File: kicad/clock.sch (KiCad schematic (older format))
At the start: 26 parts, among them SW1 SW_Push, SW2 SW_SPDT, U10 74LS08, U11 74LS04, U12 74LS32, U13 74LS08, U14 74LS04, U15 74LS08, U16 74LS04, U7 LM555, U8 LM555, U9 LM555

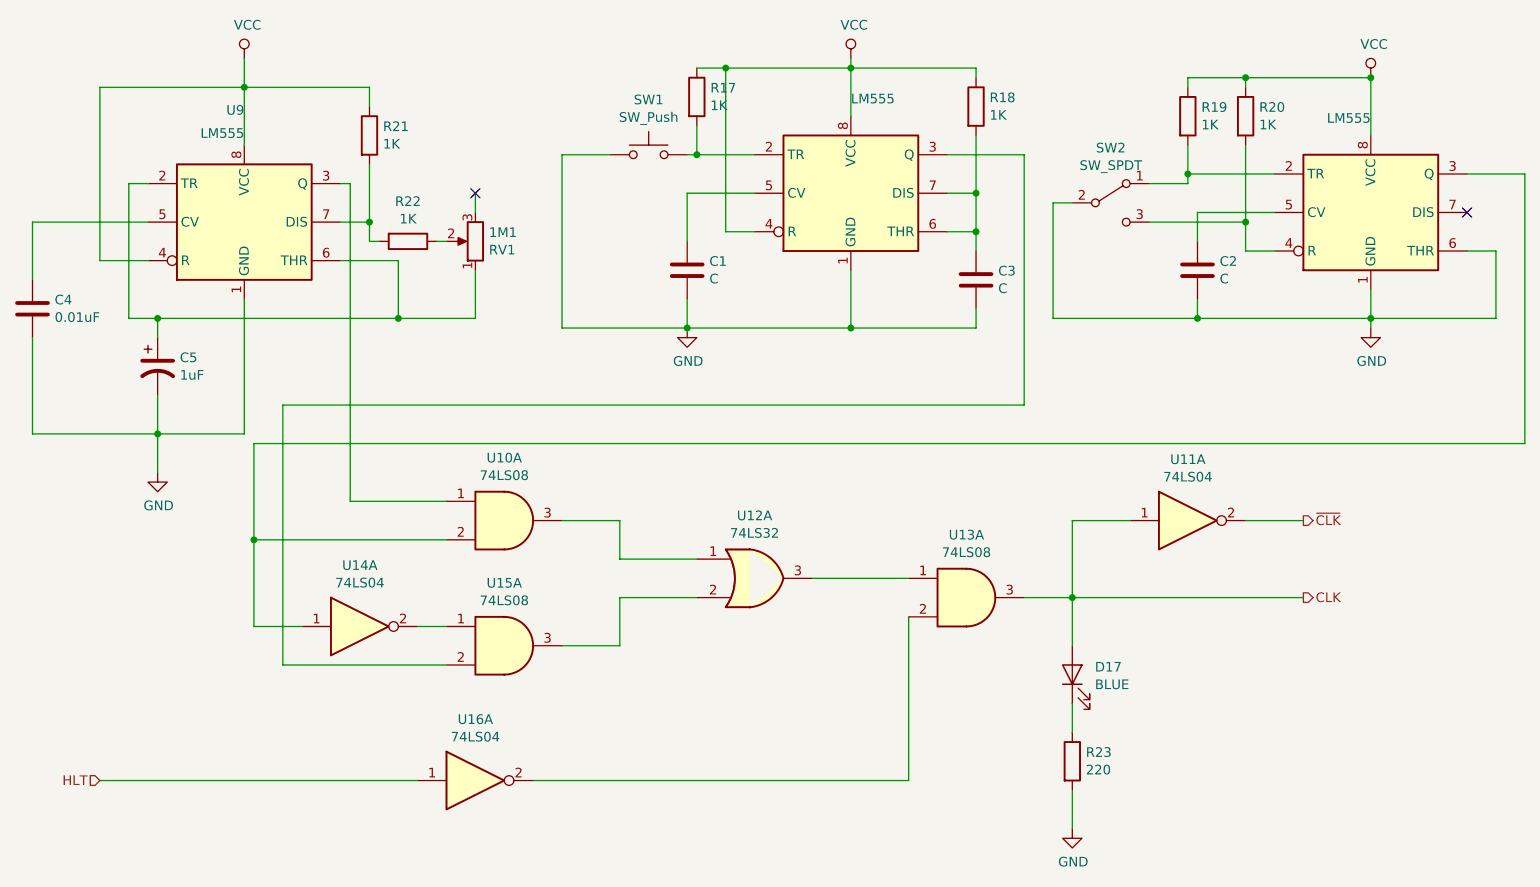
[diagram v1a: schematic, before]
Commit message: Reorganize part references
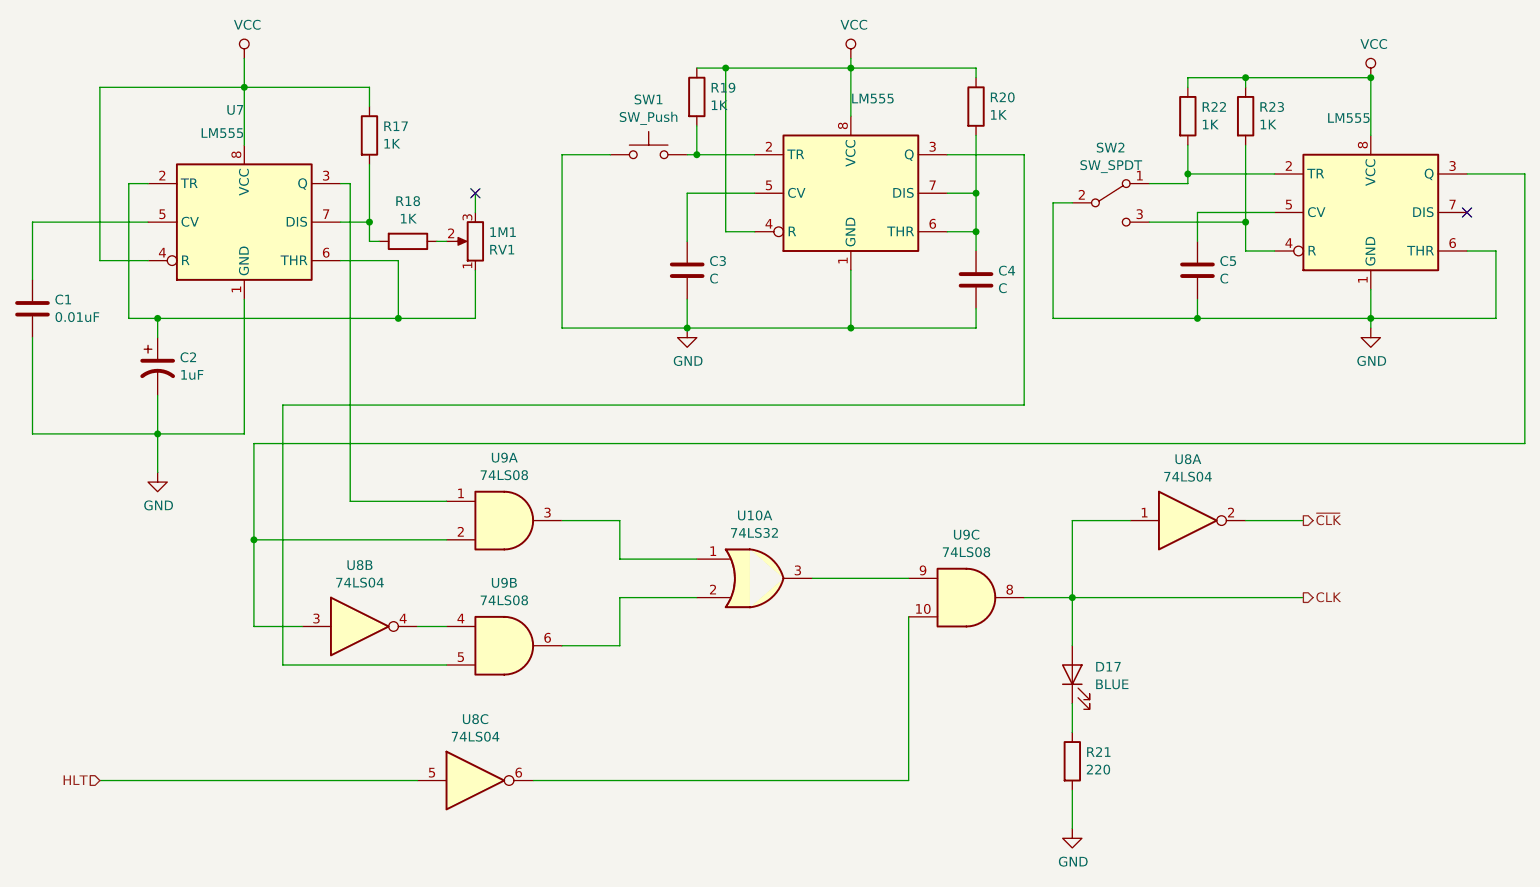
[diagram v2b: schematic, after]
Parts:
- renumbered C4 to C1, C5 to C2, C1 to C3, C3 to C4, C2 to C5, R21 to R17, R22 to R18, R17 to R19, R18 to R20, R23 to R21, R19 to R22, R20 to R23, U12 to U10, U7 to U11, U8 to U12, U9 to U7, U16 to U8, U14 to U8, U11 to U8, U10 to U9, U15 to U9, U13 to U9
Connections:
- net CLK: now also U9.8; no longer U9.3
- net HLT: now also U8.5; no longer U8.1
- net at U11.3 (Q): now also U9.5; no longer U9.2
- net at U12.3 (Q), U9.2: now also U8.3; no longer U8.1
- net at U10.2: now also U9.6; no longer U9.3
- net at U10.3: now also U9.9; no longer U9.1
- new net: U8.4, U9.4
- new net: U8.6, U9.10
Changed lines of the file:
@@
 AR Path="/5D7B7AE3/5D8B6D3B" Ref="U?"  Part="1"
 AR Path="/5DA98D6D/5DA9A52D/5D8B6D3B" Ref="U?"  Part="1"
-AR Path="/5DA9BE9A/5D8B6D3B" Ref="U11"  Part="1"
-F 0 "U11" H 7800 4117 50  0000 C CNN
+AR Path="/5DA9BE9A/5D8B6D3B" Ref="U8"  Part="1"
+F 0 "U8" H 7800 4117 50  0000 C CNN
 F 1 "74LS04" H 7800 4026 50  0000 C CNN
 F 2 "" H 7800 3800 50  0001 C CNN
@@
 AR Path="/5D7B7AE3/5D860CC7" Ref="R?"  Part="1"
 AR Path="/5DA98D6D/5DA9A52D/5D860CC7" Ref="R?"  Part="1"
-AR Path="/5DA9BE9A/5D860CC7" Ref="R23"  Part="1"
-F 0 "R23" H 7270 5096 50  0000 L CNN
+AR Path="/5DA9BE9A/5D860CC7" Ref="R21"  Part="1"
+F 0 "R21" H 7270 5096 50  0000 L CNN
 F 1 "220" H 7270 5005 50  0000 L CNN
 F 2 "" V 7130 5050 50  0001 C CNN
@@
 $Comp
 L 74xx:74LS04 U?
-U 1 1 5D8426F0
+U 2 1 5D8426F0
 P 3500 4350
 AR Path="/5D7B7AE3/5D8426F0" Ref="U?"  Part="1"
 AR Path="/5DA98D6D/5DA9A52D/5D8426F0" Ref="U?"  Part="1"
-AR Path="/5DA9BE9A/5D8426F0" Ref="U14"  Part="1"
-F 0 "U14" H 3500 4667 50  0000 C CNN
+AR Path="/5DA9BE9A/5D8426F0" Ref="U8"  Part="2"
+F 0 "U8" H 3500 4667 50  0000 C CNN
 F 1 "74LS04" H 3500 4576 50  0000 C CNN
 F 2 "" H 3500 4350 50  0001 C CNN
 F 3 "http://www.ti.com/lit/gpn/sn74LS04" H 3500 4350 50  0001 C CNN
-	1    3500 4350
+	2    3500 4350
 	1    0    0    -1
 $EndComp
@@
 $Comp
 L 74xx:74LS04 U?
-U 1 1 5D813A37
+U 3 1 5D813A37
 P 4100 5150
 AR Path="/5D7B7AE3/5D813A37" Ref="U?"  Part="1"
 AR Path="/5DA98D6D/5DA9A52D/5D813A37" Ref="U?"  Part="1"
-AR Path="/5DA9BE9A/5D813A37" Ref="U16"  Part="1"
-F 0 "U16" H 4100 5467 50  0000 C CNN
+AR Path="/5DA9BE9A/5D813A37" Ref="U8"  Part="3"
+F 0 "U8" H 4100 5467 50  0000 C CNN
 F 1 "74LS04" H 4100 5376 50  0000 C CNN
 F 2 "" H 4100 5150 50  0001 C CNN
 F 3 "http://www.ti.com/lit/gpn/sn74LS04" H 4100 5150 50  0001 C CNN
-	1    4100 5150
+	3    4100 5150
 	1    0    0    -1
 $EndComp
 $Comp
 L 74xx:74LS08 U?
-U 1 1 5D8119E1
+U 3 1 5D8119E1
 P 6650 4200
 AR Path="/5D7B7AE3/5D8119E1" Ref="U?"  Part="1"
 AR Path="/5DA98D6D/5DA9A52D/5D8119E1" Ref="U?"  Part="1"
-AR Path="/5DA9BE9A/5D8119E1" Ref="U13"  Part="1"
-F 0 "U13" H 6650 4525 50  0000 C CNN
+AR Path="/5DA9BE9A/5D8119E1" Ref="U9"  Part="3"
+F 0 "U9" H 6650 4525 50  0000 C CNN
 F 1 "74LS08" H 6650 4434 50  0000 C CNN
 F 2 "" H 6650 4200 50  0001 C CNN
 F 3 "http://www.ti.com/lit/gpn/sn74LS08" H 6650 4200 50  0001 C CNN
-	1    6650 4200
+	3    6650 4200
 	1    0    0    -1
 $EndComp
@@
 AR Path="/5D7B7AE3/5D80F71D" Ref="U?"  Part="1"
 AR Path="/5DA98D6D/5DA9A52D/5D80F71D" Ref="U?"  Part="1"
-AR Path="/5DA9BE9A/5D80F71D" Ref="U12"  Part="1"
-F 0 "U12" H 5550 4425 50  0000 C CNN
+AR Path="/5DA9BE9A/5D80F71D" Ref="U10"  Part="1"
+F 0 "U10" H 5550 4425 50  0000 C CNN
 F 1 "74LS32" H 5550 4334 50  0000 C CNN
 F 2 "" H 5550 4100 50  0001 C CNN
@@
 $Comp
 L 74xx:74LS08 U?
-U 1 1 5D80DF64
+U 2 1 5D80DF64
 P 4250 4450
 AR Path="/5D7B7AE3/5D80DF64" Ref="U?"  Part="1"
 AR Path="/5DA98D6D/5DA9A52D/5D80DF64" Ref="U?"  Part="1"
-AR Path="/5DA9BE9A/5D80DF64" Ref="U15"  Part="1"
-F 0 "U15" H 4250 4775 50  0000 C CNN
+AR Path="/5DA9BE9A/5D80DF64" Ref="U9"  Part="2"
+F 0 "U9" H 4250 4775 50  0000 C CNN
 F 1 "74LS08" H 4250 4684 50  0000 C CNN
 F 2 "" H 4250 4450 50  0001 C CNN
 F 3 "http://www.ti.com/lit/gpn/sn74LS08" H 4250 4450 50  0001 C CNN
-	1    4250 4450
+	2    4250 4450
 	1    0    0    -1
 $EndComp
@@
 AR Path="/5D7B7AE3/5D8098EF" Ref="U?"  Part="1"
 AR Path="/5DA98D6D/5DA9A52D/5D8098EF" Ref="U?"  Part="1"
-AR Path="/5DA9BE9A/5D8098EF" Ref="U10"  Part="1"
-F 0 "U10" H 4250 4125 50  0000 C CNN
+AR Path="/5DA9BE9A/5D8098EF" Ref="U9"  Part="1"
+F 0 "U9" H 4250 4125 50  0000 C CNN
 F 1 "74LS08" H 4250 4034 50  0000 C CNN
 F 2 "" H 4250 3800 50  0001 C CNN
@@
 AR Path="/5D7B7AE3/5D7DD2EC" Ref="C?"  Part="1"
 AR Path="/5DA98D6D/5DA9A52D/5D7DD2EC" Ref="C?"  Part="1"
-AR Path="/5DA9BE9A/5D7DD2EC" Ref="C2"  Part="1"
-F 0 "C2" H 7965 2546 50  0000 L CNN
+AR Path="/5DA9BE9A/5D7DD2EC" Ref="C5"  Part="1"
+F 0 "C5" H 7965 2546 50  0000 L CNN
 F 1 "C" H 7965 2455 50  0000 L CNN
 F 2 "" H 7888 2350 50  0001 C CNN
@@
 AR Path="/5D7B7AE3/5D7DD2C1" Ref="R?"  Part="1"
 AR Path="/5DA98D6D/5DA9A52D/5D7DD2C1" Ref="R?"  Part="1"
-AR Path="/5DA9BE9A/5D7DD2C1" Ref="R19"  Part="1"
-F 0 "R19" H 7870 1746 50  0000 L CNN
+AR Path="/5DA9BE9A/5D7DD2C1" Ref="R22"  Part="1"
+F 0 "R22" H 7870 1746 50  0000 L CNN
 F 1 "1K" H 7870 1655 50  0000 L CNN
 F 2 "" V 7730 1700 50  0001 C CNN
@@
 AR Path="/5D7B7AE3/5D7DD2BB" Ref="R?"  Part="1"
 AR Path="/5DA98D6D/5DA9A52D/5D7DD2BB" Ref="R?"  Part="1"
-AR Path="/5DA9BE9A/5D7DD2BB" Ref="R20"  Part="1"
-F 0 "R20" H 8170 1746 50  0000 L CNN
+AR Path="/5DA9BE9A/5D7DD2BB" Ref="R23"  Part="1"
+F 0 "R23" H 8170 1746 50  0000 L CNN
 F 1 "1K" H 8170 1655 50  0000 L CNN
 F 2 "" V 8030 1700 50  0001 C CNN
@@
 AR Path="/5D7B7AE3/5D7DD2B1" Ref="R?"  Part="1"
 AR Path="/5DA98D6D/5DA9A52D/5D7DD2B1" Ref="R?"  Part="1"
-AR Path="/5DA9BE9A/5D7DD2B1" Ref="R18"  Part="1"
-F 0 "R18" H 6770 1696 50  0000 L CNN
+AR Path="/5DA9BE9A/5D7DD2B1" Ref="R20"  Part="1"
+F 0 "R20" H 6770 1696 50  0000 L CNN
 F 1 "1K" H 6770 1605 50  0000 L CNN
 F 2 "" V 6630 1650 50  0001 C CNN
@@
 AR Path="/5D7B7AE3/5D7DD2A0" Ref="C?"  Part="1"
 AR Path="/5DA98D6D/5DA9A52D/5D7DD2A0" Ref="C?"  Part="1"
-AR Path="/5DA9BE9A/5D7DD2A0" Ref="C1"  Part="1"
-F 0 "C1" H 5315 2546 50  0000 L CNN
+AR Path="/5DA9BE9A/5D7DD2A0" Ref="C3"  Part="1"
+F 0 "C3" H 5315 2546 50  0000 L CNN
 F 1 "C" H 5315 2455 50  0000 L CNN
 F 2 "" H 5238 2350 50  0001 C CNN
@@
 AR Path="/5D7B7AE3/5D7DD29A" Ref="C?"  Part="1"
 AR Path="/5DA98D6D/5DA9A52D/5D7DD29A" Ref="C?"  Part="1"
-AR Path="/5DA9BE9A/5D7DD29A" Ref="C3"  Part="1"
-F 0 "C3" H 6815 2596 50  0000 L CNN
+AR Path="/5DA9BE9A/5D7DD29A" Ref="C4"  Part="1"
+F 0 "C4" H 6815 2596 50  0000 L CNN
 F 1 "C" H 6815 2505 50  0000 L CNN
 F 2 "" H 6738 2400 50  0001 C CNN
@@
 AR Path="/5D7B7AE3/5D7DD27E" Ref="R?"  Part="1"
 AR Path="/5DA98D6D/5DA9A52D/5D7DD27E" Ref="R?"  Part="1"
-AR Path="/5DA9BE9A/5D7DD27E" Ref="R17"  Part="1"
-F 0 "R17" H 5320 1646 50  0000 L CNN
+AR Path="/5DA9BE9A/5D7DD27E" Ref="R19"  Part="1"
+F 0 "R19" H 5320 1646 50  0000 L CNN
 F 1 "1K" H 5320 1555 50  0000 L CNN
 F 2 "" V 5180 1600 50  0001 C CNN
@@
 AR Path="/5D7B7AE3/5D7DD266" Ref="C?"  Part="1"
 AR Path="/5DA98D6D/5DA9A52D/5D7DD266" Ref="C?"  Part="1"
-AR Path="/5DA9BE9A/5D7DD266" Ref="C5"  Part="1"
-F 0 "C5" H 2565 3046 50  0000 L CNN
+AR Path="/5DA9BE9A/5D7DD266" Ref="C2"  Part="1"
+F 0 "C2" H 2565 3046 50  0000 L CNN
 F 1 "1uF" H 2565 2955 50  0000 L CNN
 F 2 "" H 2450 3000 50  0001 C CNN
@@
 AR Path="/5D7B7AE3/5D7DD258" Ref="C?"  Part="1"
 AR Path="/5DA98D6D/5DA9A52D/5D7DD258" Ref="C?"  Part="1"
-AR Path="/5DA9BE9A/5D7DD258" Ref="C4"  Part="1"
-F 0 "C4" H 1915 2746 50  0000 L CNN
+AR Path="/5DA9BE9A/5D7DD258" Ref="C1"  Part="1"
+F 0 "C1" H 1915 2746 50  0000 L CNN
 F 1 "0.01uF" H 1915 2655 50  0000 L CNN
 F 2 "" H 1838 2550 50  0001 C CNN
@@
 AR Path="/5D7B7AE3/5D7DD239" Ref="R?"  Part="1"
 AR Path="/5DA98D6D/5DA9A52D/5D7DD239" Ref="R?"  Part="1"
-AR Path="/5DA9BE9A/5D7DD239" Ref="R22"  Part="1"
-F 0 "R22" V 3543 2350 50  0000 C CNN
+AR Path="/5DA9BE9A/5D7DD239" Ref="R18"  Part="1"
+F 0 "R18" V 3543 2350 50  0000 C CNN
 F 1 "1K" V 3634 2350 50  0000 C CNN
 F 2 "" V 3680 2350 50  0001 C CNN
@@
 AR Path="/5D7B7AE3/5D7DD233" Ref="R?"  Part="1"
 AR Path="/5DA98D6D/5DA9A52D/5D7DD233" Ref="R?"  Part="1"
-AR Path="/5DA9BE9A/5D7DD233" Ref="R21"  Part="1"
-F 0 "R21" H 3620 1846 50  0000 L CNN
+AR Path="/5DA9BE9A/5D7DD233" Ref="R17"  Part="1"
+F 0 "R17" H 3620 1846 50  0000 L CNN
 F 1 "1K" H 3620 1755 50  0000 L CNN
 F 2 "" V 3480 1800 50  0001 C CNN
@@
 AR Path="/5D7B7AE3/5D7DD215" Ref="U?"  Part="1"
 AR Path="/5DA98D6D/5DA9A52D/5D7DD215" Ref="U?"  Part="1"
-AR Path="/5DA9BE9A/5D7DD215" Ref="U8"  Part="1"
-F 0 "U8" H 8750 2781 50  0001 C CNN
+AR Path="/5DA9BE9A/5D7DD215" Ref="U12"  Part="1"
+F 0 "U12" H 8750 2781 50  0001 C CNN
 F 1 "LM555" H 8750 2689 50  0000 R CNN
 F 2 "" H 8750 2200 50  0001 C CNN
@@
 AR Path="/5D7B7AE3/5D7DD20F" Ref="U?"  Part="1"
 AR Path="/5DA98D6D/5DA9A52D/5D7DD20F" Ref="U?"  Part="1"
-AR Path="/5DA9BE9A/5D7DD20F" Ref="U7"  Part="1"
-F 0 "U7" H 6050 2681 50  0001 C CNN
+AR Path="/5DA9BE9A/5D7DD20F" Ref="U11"  Part="1"
+F 0 "U11" H 6050 2681 50  0001 C CNN
 F 1 "LM555" H 6050 2590 50  0000 L CNN
 F 2 "" H 6050 2100 50  0001 C CNN
@@
 AR Path="/5D7B7AE3/5D7DD209" Ref="U?"  Part="1"
 AR Path="/5DA98D6D/5DA9A52D/5D7DD209" Ref="U?"  Part="1"
-AR Path="/5DA9BE9A/5D7DD209" Ref="U9"  Part="1"
-F 0 "U9" H 2900 2831 50  0000 R CNN
+AR Path="/5DA9BE9A/5D7DD209" Ref="U7"  Part="1"
+F 0 "U7" H 2900 2831 50  0000 R CNN
 F 1 "LM555" H 2900 2740 50  0000 R TNN
 F 2 "" H 2900 2250 50  0001 C CNN
